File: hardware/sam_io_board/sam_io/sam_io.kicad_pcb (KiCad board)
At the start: 2 copper layers, 100 x 100 mm, 104 parts, among them J1 Conn_01x06, J2 nmount JST 1mm QWIIC, J3 nmount SW Debug, J4 USB_C_Receptacle_USB2.0, J5 Conn_01x06, J9 SAM BUS, Q1 2N7002, SW1 Reset, SW2 Boot, SW3 ADDRESS, U1 ADM3483, U2 W25Q128JVSIQ, U3 RP2040, U4 LMV321, U5 SN74AHCT1G125, U6 AP2112K-3.3, U7 SN74LVC8T245, U8 74AHCT541, Y1 12MHz,18pF

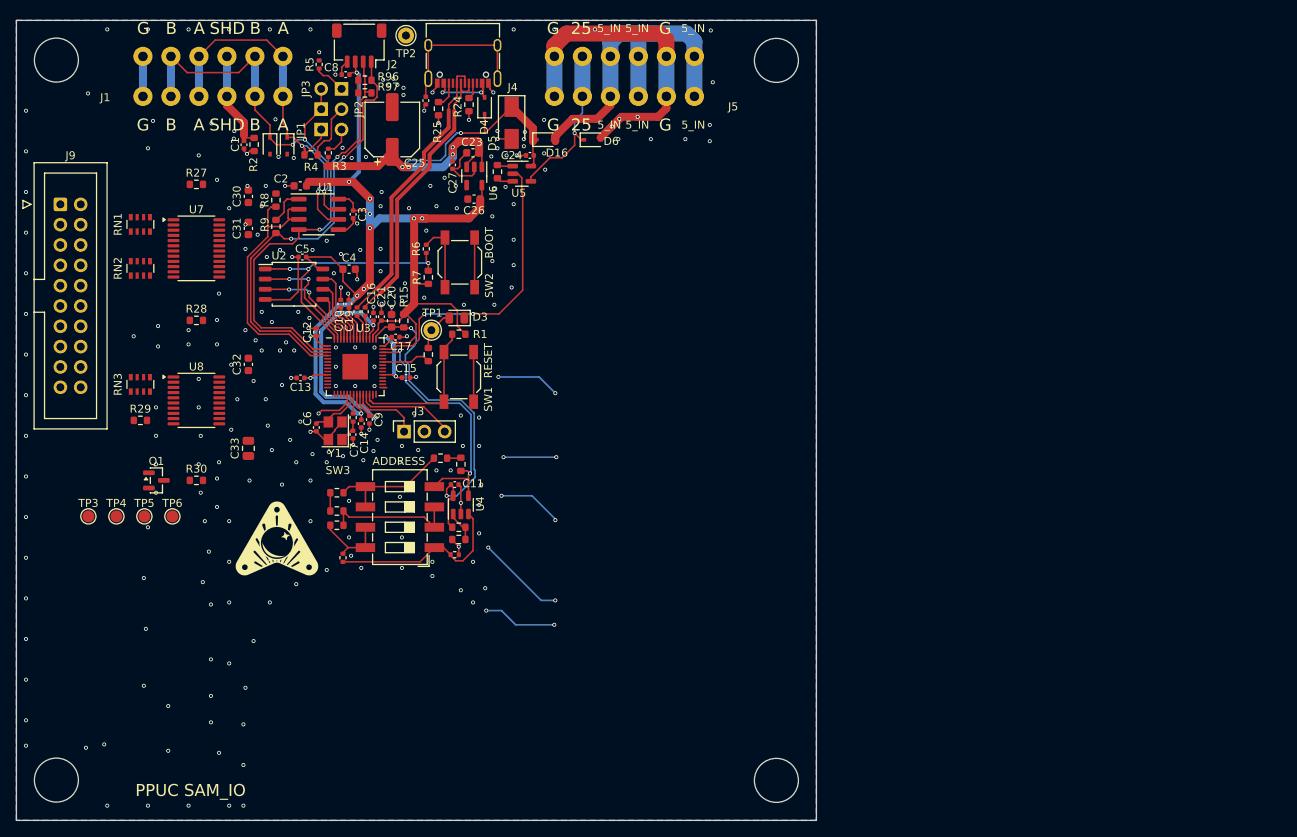
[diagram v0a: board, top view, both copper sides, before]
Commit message: SAM_IO board: 100 x 70 mm outline, SAM bus routed on two layers
Cuts the board to Opto_16 size plus the 2.7 mm SW3 needs, places the SAM
bus parts next to the RP2040 and routes them: the RP2040 side by hand
(each bus line flips through two vias, since both ends number their pins
anticlockwise), the J9 side, pull-ups and power with Freerouting, then
touch-ups. DRC: no unconnected item, no new violation.

Co-Authored-By: Claude Opus 5.5 (1M context) <noreply@anthropic.com>
Claude-Session: https://claude.ai/code/session_018thCiq9Wkjwqc7njbZAM79
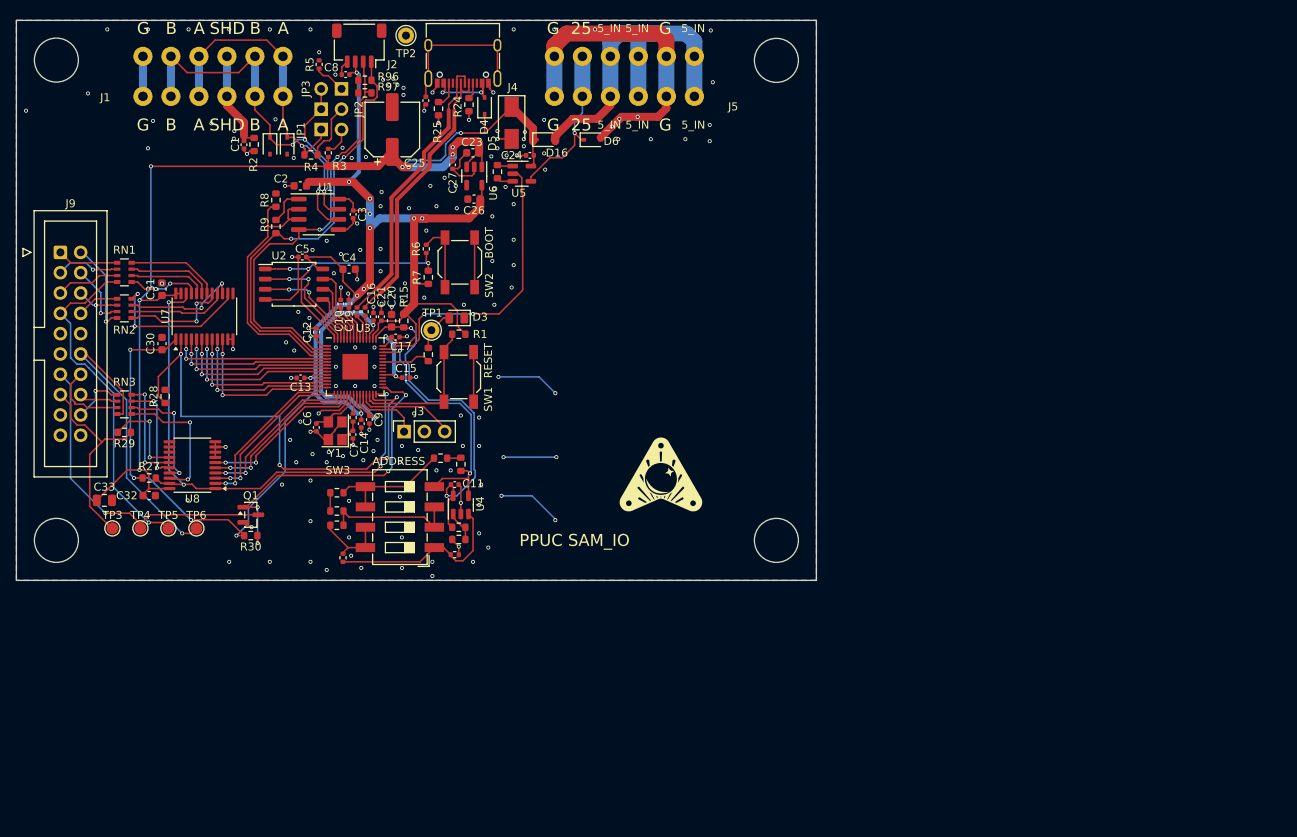
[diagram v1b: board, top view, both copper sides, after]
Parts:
- moved R27 37.2 mm to (91.6, 96.2)
- moved REF** 30.0 mm to (170.0, 104.0)
- moved REF** 30.0 mm to (80.0, 104.0)
- moved C30 21.3 mm to (93.2, 79.4)
- moved C32 20.6 mm to (91.6, 98.4), turned to 0 degrees
- moved C33 19.1 mm to (86.0, 99.0), turned to 0 degrees
- moved C31 13.2 mm to (93.2, 72.6)
- moved Q1 12.6 mm to (104.3, 100.8)
- moved R28 10.3 mm to (93.6, 86.0), turned to 90 degrees
- moved R30 9.69 mm to (104.3, 103.4)
- moved U7 8.56 mm to (98.5, 76.0), turned to 90 degrees
- moved U8 8.12 mm to (97.0, 94.6), turned to 180 degrees
- moved RN1 6.32 mm to (88.5, 70.5), turned to 0 degrees
- moved J9 6.00 mm to (80.5, 68.0)
- moved RN2 5.39 mm to (88.5, 75.0), turned to 0 degrees
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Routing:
- net +5V: track 61.1 -> 141.6 mm, vias 5 -> 8
- net BUS_OE_N: track 0.00 -> 67.2 mm, vias 0 -> 4
- net +3V3: track 166.1 -> 230.2 mm, vias 14 -> 18
- net BUS_DIR: track 0.53 -> 62.3 mm, vias 0 -> 4
- net Net-(J9-Pin_7): track 0.00 -> 42.8 mm, vias 0 -> 1
- net NBRESET_DRV: track 0.51 -> 41.1 mm, vias 0 -> 4
- net Net-(J9-Pin_12): track 0.00 -> 40.5 mm, vias 0 -> 1
- net Net-(J9-Pin_13): track 0.00 -> 40.4 mm, vias 0 -> 1
- net Net-(J9-Pin_15): track 0.00 -> 25.4 mm
- net BUS_A0: track 0.00 -> 21.1 mm, vias 0 -> 2
- net BUS_A1: track 0.00 -> 21.0 mm, vias 0 -> 2
- net BUS_A2: track 0.00 -> 20.9 mm, vias 0 -> 2
- net BUS_A3: track 0.00 -> 20.8 mm, vias 0 -> 2
- net BUS_D7: track 0.00 -> 20.7 mm, vias 0 -> 2
- net BUS_IOSTB: track 0.00 -> 20.6 mm, vias 0 -> 2
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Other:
- board size 100 x 100 mm -> 100 x 70 mm

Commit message: SAM_IO: remove the QWIIC option (J2, R96, R97, C8); R9 becomes a track
Schematic: J2 and its pull-ups and decoupling removed, the 0 ohm R9 (U1 RO to GPIO1) replaced by a wire.
../sam_io board: the parts and their stubs removed. R9 cannot be a straight track because /485_DE runs
between its pads, so RO hops through one via on B.Cu to the existing /485_RX via. DRC: 0 unconnected,
0 clearance, schematic parity clean apart from the existing field differences.
sam_io_krt (0.15 mm) board: same removal, R9 as a straight F.Cu track, DRC unchanged.

Co-Authored-By: Claude Opus 5.5 (1M context) <noreply@anthropic.com>
Claude-Session: https://claude.ai/code/session_012ePkTGNjii74e9emvMVPmF
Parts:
- removed C8: 100n, Capacitor_SMD:C_0402_1005Metric
- removed J2: nmount JST 1mm QWIIC, Connector_JST:JST_SH_SM04B-SRSS-TB_1x04-1MP_P1.00mm_Horizontal
- removed R9: 0, Resistor_SMD:R_0603_1608Metric
- removed R96, R97: 10k, Resistor_SMD:R_0603_1608Metric
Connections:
- U1 pad 1: Net-(U1-RO) -> /485_RX
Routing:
- net /485_TX: track 53.5 -> 38.9 mm
- net /485_RX: track 55.7 -> 47.8 mm, vias 2 -> 3
- net Net-(U1-RO): track 4.68 -> 0.00 mm
- net +3V3: track 230.2 -> 225.5 mm
- net GND: track 151.6 -> 149.7 mm

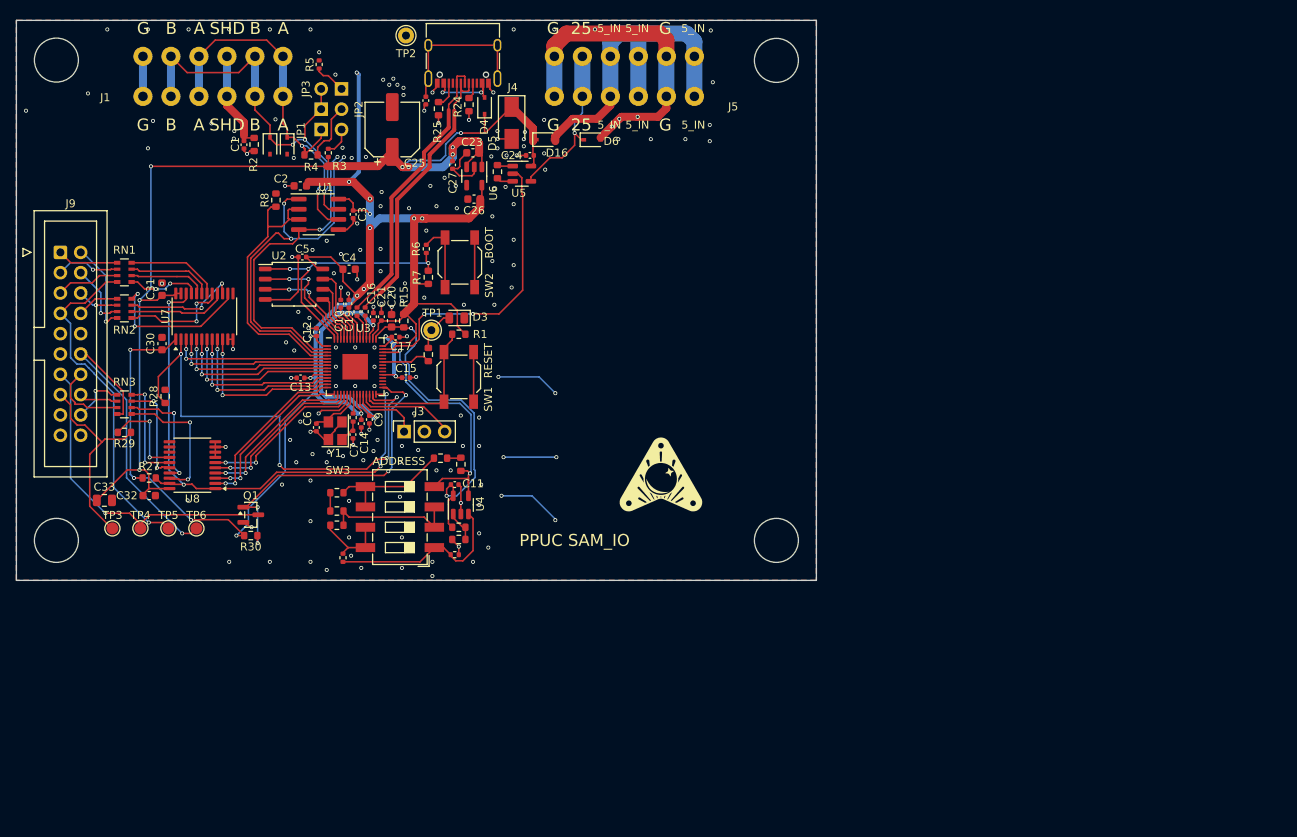
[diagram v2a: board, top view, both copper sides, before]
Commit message: SAM_IO rev 0.2: place and route the PCB (100 x 100 mm)
RP2354B, its core regulator and the dedicated-switch harness connectors
J2/J3/J13 with their 17 input stages placed and routed. Outline grown down
by 30 mm. DRC: no unconnected item, only rev 0.1's J4 errors left. Hole
clearance rule 0.25 mm. Renders, docs and the scripts used (tools/rev02).

Co-Authored-By: Claude Opus 5.5 (1M context) <noreply@anthropic.com>
Claude-Session: https://claude.ai/code/session_01Mh8jyzQSZ4SYbwGJXqcn3P
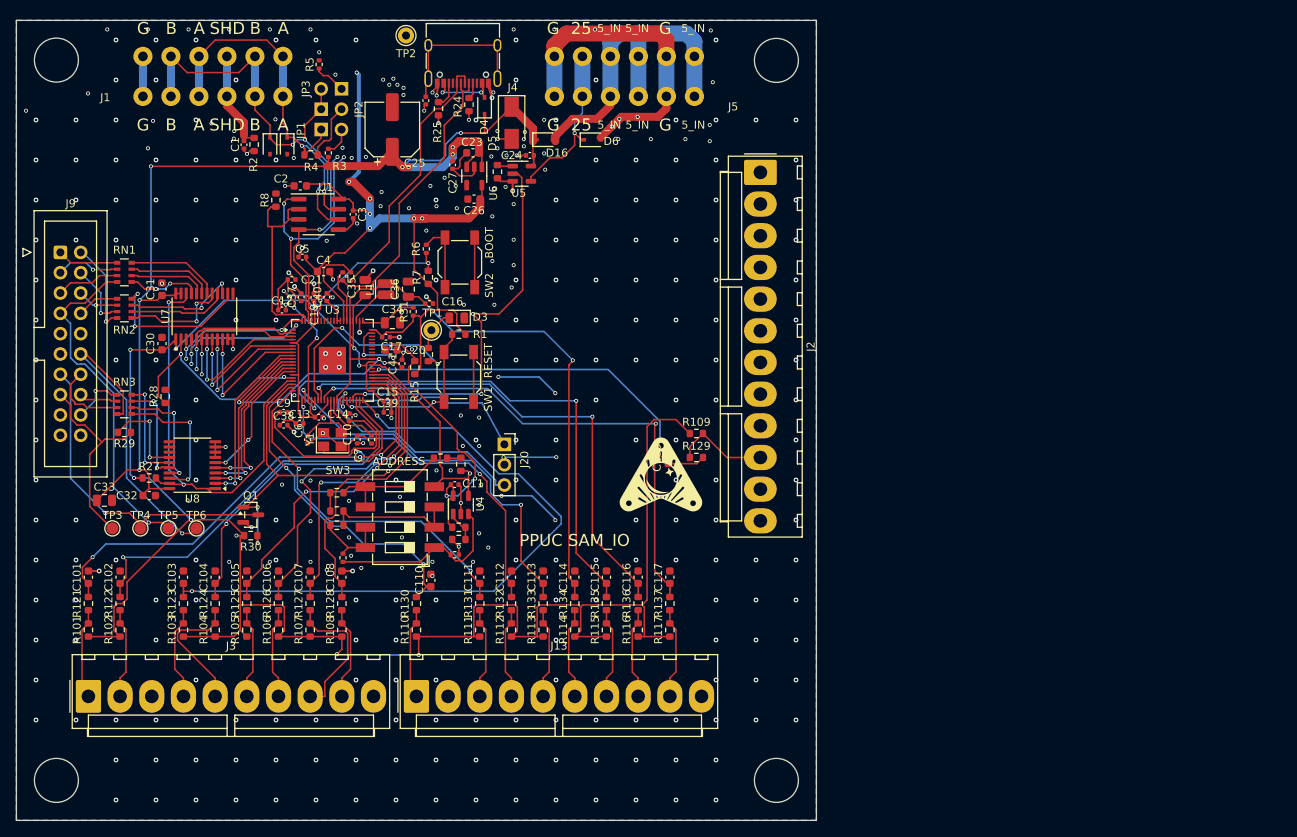
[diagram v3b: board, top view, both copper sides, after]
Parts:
- removed U2: W25Q128JVSIQ, Package_SO:SOIC-8_5.23x5.23mm_P1.27mm
- added C101: 1n, Capacitor_SMD:C_0603_1608Metric, F.Cu at (84.0, 108.6)
- added C102: 1n, Capacitor_SMD:C_0603_1608Metric, F.Cu at (88.0, 108.6)
- added C103: 1n, Capacitor_SMD:C_0603_1608Metric, F.Cu at (95.9, 108.6)
- added C104: 1n, Capacitor_SMD:C_0603_1608Metric, F.Cu at (99.8, 108.6)
- added C105: 1n, Capacitor_SMD:C_0603_1608Metric, F.Cu at (103.8, 108.6)
- added C106: 1n, Capacitor_SMD:C_0603_1608Metric, F.Cu at (107.8, 108.6)
- added C107: 1n, Capacitor_SMD:C_0603_1608Metric, F.Cu at (111.7, 108.6)
- added C108: 1n, Capacitor_SMD:C_0603_1608Metric, F.Cu at (115.7, 108.6)
- added C109: 1n, Capacitor_SMD:C_0603_1608Metric, F.Cu at (156.5, 93.6)
- added C110: 1n, Capacitor_SMD:C_0603_1608Metric, F.Cu at (126.8, 109.0)
- added C111: 1n, Capacitor_SMD:C_0603_1608Metric, F.Cu at (132.9, 108.6)
- added C112: 1n, Capacitor_SMD:C_0603_1608Metric, F.Cu at (136.9, 108.6)
- added C113: 1n, Capacitor_SMD:C_0603_1608Metric, F.Cu at (140.8, 108.6)
- added C114: 1n, Capacitor_SMD:C_0603_1608Metric, F.Cu at (144.8, 108.6)
- added C115: 1n, Capacitor_SMD:C_0603_1608Metric, F.Cu at (148.8, 108.6)
- added C116: 1n, Capacitor_SMD:C_0603_1608Metric, F.Cu at (152.7, 108.6)
- added C117: 1n, Capacitor_SMD:C_0603_1608Metric, F.Cu at (156.7, 108.6)
- added C34: 4.7u, Capacitor_SMD:C_0805_2012Metric, F.Cu at (122.0, 76.8)
- added C35: 4.7u, Capacitor_SMD:C_0805_2012Metric, F.Cu at (118.6, 72.4)
- added C36: 4.7u, Capacitor_SMD:C_0805_2012Metric, F.Cu at (124.0, 72.6)
- added C37: 100n, Capacitor_SMD:C_0402_1005Metric, F.Cu at (110.6, 73.6)
- added C38: 100n, Capacitor_SMD:C_0402_1005Metric, F.Cu at (108.4, 89.6)
- added C39: 100n, Capacitor_SMD:C_0402_1005Metric, F.Cu at (121.4, 88.0)
- added C40: 100n, Capacitor_SMD:C_0402_1005Metric, F.Cu at (113.8, 73.6)
- added C41: 100n, Capacitor_SMD:C_0402_1005Metric, F.Cu at (123.2, 81.9)
- added J13: J13 DEDICATED D17-D24, Connector_Molex:Molex_KK-396_A-41791-0010_1x10_P3.96mm_Vertical, F.Cu at (125.0, 123.5)
- added J2: J2 DEDICATED D1-D8, Connector_Molex:Molex_KK-396_A-41791-0012_1x12_P3.96mm_Vertical, F.Cu at (168.0, 58.0)
- added J3: J3 DEDICATED D9-D16, Connector_Molex:Molex_KK-396_A-41791-0010_1x10_P3.96mm_Vertical, F.Cu at (84.0, 123.5)
- added L1: 3.3u, Inductor_SMD:L_Cenker_CKCS201610, F.Cu at (121.2, 72.6)
- added R101: 1k, Resistor_SMD:R_0603_1608Metric, F.Cu at (84.0, 115.2)
- added R102: 1k, Resistor_SMD:R_0603_1608Metric, F.Cu at (88.0, 115.2)
- added R103: 1k, Resistor_SMD:R_0603_1608Metric, F.Cu at (95.9, 115.2)
- added R104: 1k, Resistor_SMD:R_0603_1608Metric, F.Cu at (99.8, 115.2)
- added R105: 1k, Resistor_SMD:R_0603_1608Metric, F.Cu at (103.8, 115.2)
- added R106: 1k, Resistor_SMD:R_0603_1608Metric, F.Cu at (107.8, 115.2)
- added R107: 1k, Resistor_SMD:R_0603_1608Metric, F.Cu at (111.7, 115.2)
- added R108: 1k, Resistor_SMD:R_0603_1608Metric, F.Cu at (115.7, 115.2)
- added R109: 1k, Resistor_SMD:R_0603_1608Metric, F.Cu at (160.0, 90.6)
- added R110: 1k, Resistor_SMD:R_0603_1608Metric, F.Cu at (125.0, 115.2)
- added R111: 1k, Resistor_SMD:R_0603_1608Metric, F.Cu at (132.9, 115.2)
- added R112: 1k, Resistor_SMD:R_0603_1608Metric, F.Cu at (136.9, 115.2)
- added R113: 1k, Resistor_SMD:R_0603_1608Metric, F.Cu at (140.8, 115.2)
- added R114: 1k, Resistor_SMD:R_0603_1608Metric, F.Cu at (144.8, 115.2)
- added R115: 1k, Resistor_SMD:R_0603_1608Metric, F.Cu at (148.8, 115.2)
- added R116: 1k, Resistor_SMD:R_0603_1608Metric, F.Cu at (152.7, 115.2)
- added R117: 1k, Resistor_SMD:R_0603_1608Metric, F.Cu at (156.7, 115.2)
- added R121: 10k, Resistor_SMD:R_0603_1608Metric, F.Cu at (84.0, 111.9)
- added R122: 10k, Resistor_SMD:R_0603_1608Metric, F.Cu at (88.0, 111.9)
- added R123: 10k, Resistor_SMD:R_0603_1608Metric, F.Cu at (95.9, 111.9)
- added R124: 10k, Resistor_SMD:R_0603_1608Metric, F.Cu at (99.8, 111.9)
- added R125: 10k, Resistor_SMD:R_0603_1608Metric, F.Cu at (103.8, 111.9)
- added R126: 10k, Resistor_SMD:R_0603_1608Metric, F.Cu at (107.8, 111.9)
- added R127: 10k, Resistor_SMD:R_0603_1608Metric, F.Cu at (111.7, 111.9)
- added R128: 10k, Resistor_SMD:R_0603_1608Metric, F.Cu at (115.7, 111.9)
- added R129: 10k, Resistor_SMD:R_0603_1608Metric, F.Cu at (160.0, 93.6)
- added R130: 10k, Resistor_SMD:R_0603_1608Metric, F.Cu at (125.0, 111.9)
- added R131: 10k, Resistor_SMD:R_0603_1608Metric, F.Cu at (132.9, 111.9)
- added R132: 10k, Resistor_SMD:R_0603_1608Metric, F.Cu at (136.9, 111.9)
- added R133: 10k, Resistor_SMD:R_0603_1608Metric, F.Cu at (140.8, 111.9)
- added R134: 10k, Resistor_SMD:R_0603_1608Metric, F.Cu at (144.8, 111.9)
- added R135: 10k, Resistor_SMD:R_0603_1608Metric, F.Cu at (148.8, 111.9)
- added R136: 10k, Resistor_SMD:R_0603_1608Metric, F.Cu at (152.7, 111.9)
- added R137: 10k, Resistor_SMD:R_0603_1608Metric, F.Cu at (156.7, 111.9)
- added R31: 33, Resistor_SMD:R_0402_1005Metric, F.Cu at (124.6, 75.4)
- U3: value RP2040 -> RP2354B; footprint Package_DFN_QFN:QFN-56-1EP_7x7mm_P0.4mm_EP3.2x3.2mm -> Package_DFN_QFN:QFN-80-1EP_10x10mm_P0.4mm_EP3.4x3.4mm
- moved REF** 30.0 mm to (80.0, 134.0)
- moved REF** 30.0 mm to (170.0, 134.0)
- moved C10 14.2 mm to (116.6, 88.6)
- moved J20 12.6 mm to (136.0, 92.0), turned to 0 degrees
- moved C21 12.1 mm to (109.4, 71.4), turned to 0 degrees
- moved C9 10.8 mm to (108.4, 88.0), turned to 0 degrees
- moved C16 7.17 mm to (126.6, 74.4), turned to 0 degrees
- moved R15 6.01 mm to (124.8, 82.4), turned to 90 degrees
- moved C13 5.71 mm to (110.4, 89.4), turned to 0 degrees
- moved C14 5.37 mm to (112.8, 88.6), turned to 0 degrees
- moved R11 5.22 mm to (115.8, 71.0), turned to 90 degrees
- moved C12 5.14 mm to (108.2, 75.2), turned to 0 degrees
- moved R10 4.48 mm to (116.8, 71.0), turned to 90 degrees
- moved C19 4.44 mm to (112.2, 73.6)
- moved C15 3.74 mm to (121.4, 86.6)
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- renumbered J3 to J20
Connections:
- C6 pad 2: Net-(U3-XIN) -> /XIN
- J20 pad 1: Net-(J3-Pin_1) -> /SWCLK
- J20 pad 3: Net-(J3-Pin_3) -> /SWDIO
- R10 pad 2: Net-(U3-USB_DP) -> /USB_DP_MCU
- R11 pad 2: Net-(U3-USB_DM) -> /USB_DM_MCU
- R12 pad 2: Net-(U3-XOUT) -> /XOUT
- U3 pad 1: +3V3 -> BUS_D1
- U3 pad 10: +3V3 -> /1V1
- U3 pad 11: BUS_D5 -> BUS_A1
- U3 pad 12: BUS_D6 -> BUS_A2
- U3 pad 13: BUS_D7 -> BUS_A3
- U3 pad 14: BUS_A0 -> BUS_IOSTB
- U3 pad 15: BUS_A1 -> +3V3
- U3 pad 16: BUS_A2 -> BUS_DIR
- U3 pad 17: BUS_A3 -> BUS_OE_N
- U3 pad 18: BUS_IOSTB -> NBRESET_DRV
- U3 pad 19: GND -> DED_D17
- U3 pad 2: /485_TX -> BUS_D2
- U3 pad 20: Net-(U3-XIN) -> DED_D18
- U3 pad 21: Net-(U3-XOUT) -> DED_D19
- U3 pad 22: +3V3 -> DED_D20
- U3 pad 23: /1V1 -> DED_D21
- U3 pad 24: Net-(J3-Pin_1) -> +3V3
- U3 pad 25: Net-(J3-Pin_3) -> DED_D22
- U3 pad 26: /nReset -> Net-(U3-GPIO25)
- U3 pad 27: BUS_DIR -> DED_D23
- U3 pad 28: BUS_OE_N -> DED_D24
- U3 pad 29: NBRESET_DRV -> +3V3
- U3 pad 3: /485_RX -> BUS_D3
- U3 pad 30: unconnected-(U3-GPIO19-Pad30) -> /XIN
- U3 pad 31: unconnected-(U3-GPIO20-Pad31) -> /XOUT
- U3 pad 32: unconnected-(U3-GPIO21-Pad32) -> /1V1
- U3 pad 33: +3V3 -> /SWCLK
- U3 pad 34: unconnected-(U3-GPIO22-Pad34) -> /SWDIO
- U3 pad 35: unconnected-(U3-GPIO23-Pad35) -> /nReset
- U3 pad 37: Net-(U3-GPIO25) -> /Out_Special
- U3 pad 38: unconnected-(U3-GPIO26_ADC0-Pad38) -> DED_D9
- U3 pad 39: unconnected-(U3-GPIO27_ADC1-Pad39) -> DED_D10
- U3 pad 4: /485_DE -> BUS_D4
- U3 pad 40: /V_addr -> DED_D11
- U3 pad 41: /Out_Special -> +3V3
- U3 pad 42: +3V3 -> DED_D12
- U3 pad 43: /3V3A -> DED_D13
- U3 pad 44: +3V3 -> DED_D14
- U3 pad 45: /1V1 -> DED_D15
- U3 pad 46: Net-(U3-USB_DM) -> DED_D16
- U3 pad 47: Net-(U3-USB_DP) -> MEM_PROTECT
- U3 pad 48: +3V3 -> unconnected-(U3-GPIO39-Pad48)
- U3 pad 49: +3V3 -> /V_addr
- U3 pad 5: BUS_D0 -> +3V3
- U3 pad 50: /1V1 -> +3V3
- U3 pad 51: Net-(U2-IO3) -> /1V1
- U3 pad 52: /Q_SCLK -> unconnected-(U3-GPIO41/ADC1-Pad52)
- U3 pad 53: Net-(U2-DI(IO0)) -> unconnected-(U3-GPIO42/ADC2-Pad53)
- U3 pad 54: Net-(U2-IO2) -> unconnected-(U3-GPIO43/ADC3-Pad54)
- U3 pad 55: Net-(U2-DO(IO1)) -> unconnected-(U3-GPIO44/ADC4-Pad55)
- U3 pad 56: /Q_nCS -> unconnected-(U3-GPIO45/ADC5-Pad56)
- U3 pad 57: GND -> unconnected-(U3-GPIO46/ADC6-Pad57)
- U3 pad 6: BUS_D1 -> BUS_D5
- U3 pad 7: BUS_D2 -> BUS_D6
- U3 pad 8: BUS_D3 -> BUS_D7
- U3 pad 9: BUS_D4 -> BUS_A0
- Y1 pad 3: Net-(U3-XIN) -> /XIN
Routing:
- net +3V3: track 225.5 -> 396.1 mm
- net DED_D21: track 0.00 -> 85.6 mm, vias 0 -> 4
- net DED_D11: track 0.00 -> 85.0 mm, vias 0 -> 2
- net DED_D24: track 0.00 -> 67.5 mm, vias 0 -> 2
- net DED_D22: track 0.00 -> 66.4 mm, vias 0 -> 2
- net DED_D23: track 0.00 -> 62.6 mm, vias 0 -> 2
- net DED_D9: track 0.00 -> 54.4 mm, vias 0 -> 2
- net DED_D10: track 0.00 -> 54.3 mm, vias 0 -> 2
- net /1V1: track 35.1 -> 86.2 mm
- net MEM_PROTECT: track 0.00 -> 49.3 mm, vias 0 -> 2
- net DED_D20: track 0.00 -> 48.3 mm, vias 0 -> 2
- net DED_D19: track 0.00 -> 45.3 mm, vias 0 -> 2
- net DED_D18: track 0.00 -> 44.4 mm, vias 0 -> 2
- net DED_D12: track 0.00 -> 44.2 mm, vias 0 -> 2
- net DED_D14: track 0.00 -> 41.8 mm, vias 0 -> 2
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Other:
- board size 100 x 70 mm -> 100 x 100 mm
